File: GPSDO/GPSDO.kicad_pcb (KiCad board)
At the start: 2 copper layers, 39.6 x 27.3 mm, 37 parts, among them J1 analog, J2 Conn_01x03_Pin, J3 USB_B_Mini, J4 1PPSin, SW1 RST#, U1 FT230XS, U2 CH32V003FxPx, U3 TLV9061xDBV, Y2 24 MHz Farnell 4165823

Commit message: 3D model
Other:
- board text added: "CH32V003 GPSDO"
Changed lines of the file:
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@@
 		(tags "SMA THT Female Jack Vertical")
 		(property "Reference" "J4"
-			(at -0.44 -4.56 90)
+			(at 2.54 -5.06 90)
 			(layer "F.SilkS")
 			(effects
@@
 		)
 		(embedded_fonts no)
-		(model "${KICAD10_3DMODEL_DIR}/Connector_Coaxial.3dshapes/SMA_Amphenol_901-144_Vertical.step"
+		(model "${KIPRJMOD}/901-144-8RFX.stp"
 			(offset
-				(xyz 0 0 0)
+				(xyz 0 0 9.5)
 			)
 			(scale
@@
 			)
 			(rotate
-				(xyz 0 0 0)
+				(xyz -0 -90 -0)
 			)
 		)
@@
 		(layer "Edge.Cuts")
 	)
+	(gr_text "CH32V003\nGPSDO"
+		(at 179.28714 83.0016 0)
+		(layer "F.SilkS")
+		(effects
+			(font
+				(size 1.2 1.2)
+				(thickness 0.25)
+				(bold yes)
+			)
+			(justify left bottom)
+		)
+	)
 	(segment

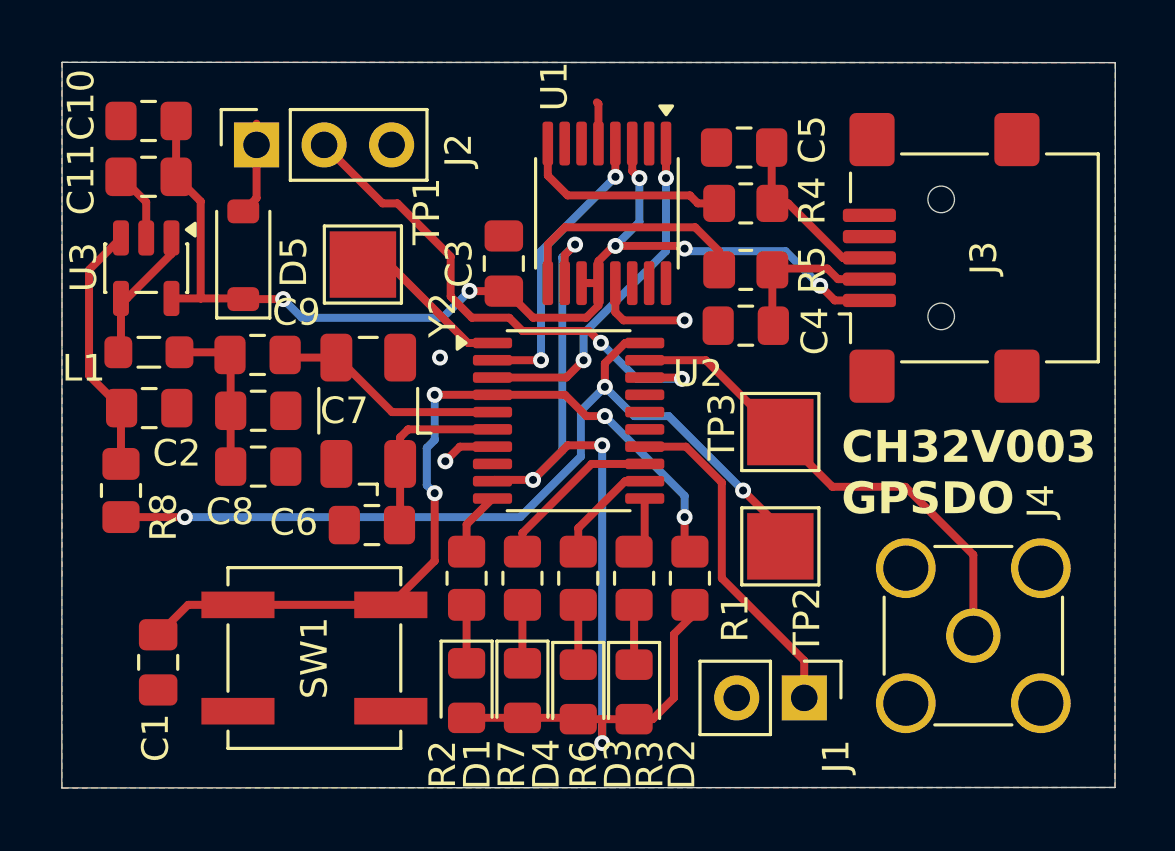
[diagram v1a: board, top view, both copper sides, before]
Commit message: add mounting holes
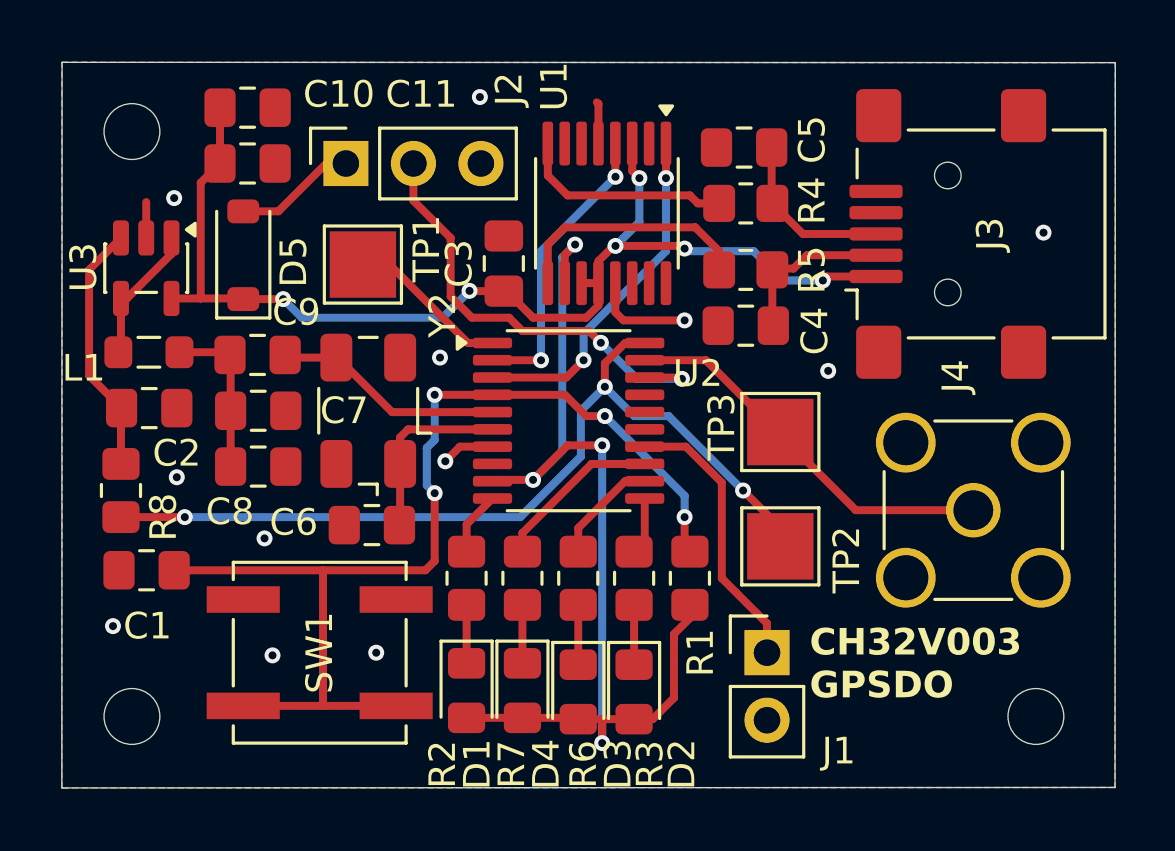
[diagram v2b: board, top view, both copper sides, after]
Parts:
- added H1: MountingHole, MountingHole:MountingHole_2.1mm, F.Cu at (152.6, 68.5)
- added H2: MountingHole, MountingHole:MountingHole_2.1mm, F.Cu at (152.6, 90.5)
- added H3: MountingHole, MountingHole:MountingHole_2.1mm, F.Cu at (186.6, 90.5)
- moved J4 4.72 mm to (184.2, 82.7)
- moved C10 3.76 mm to (156.9, 67.6), turned to 0 degrees
- moved C11 3.76 mm to (156.9, 69.7), turned to 0 degrees
- moved C1 3.49 mm to (153.1, 85.0), turned to 180 degrees
- moved J2 3.43 mm to (160.6, 69.7)
- moved J1 2.20 mm to (176.5, 88.1), turned to 0 degrees
- moved J3 0.93 mm to (183.3, 72.4)
- moved SW1 0.28 mm to (159.7, 88.1), turned to 180 degrees
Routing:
- net Net-(SW1-A): track 31.2 -> 40.5 mm
- net /IC 1PPS: track 18.4 -> 14.7 mm
- net /SWIO: track 19.4 -> 17.0 mm
- net /A2: track 12.8 -> 10.6 mm
- net GND: track 10.1 -> 8.75 mm, vias 3 -> 12

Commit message: rotate analog in
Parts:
- moved J1 3.30 mm to (176.5, 91.4), turned to 90 degrees
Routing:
- net /A2: track 10.6 -> 13.9 mm
- net GND: track 8.75 -> 10.1 mm, vias 12 -> 14
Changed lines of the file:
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@@
 	(footprint "Connector_PinHeader_2.54mm:PinHeader_1x02_P2.54mm_Vertical"
 		(layer "F.Cu")
-		(at 176.48714 88.1016)
+		(at 176.48714 91.4016 90)
 		(descr "Through hole straight pin header, 1x02, 2.54mm pitch, single row")
 		(tags "Through hole pin header THT 1x02 2.54mm single row")
 		(property "Reference" "J1"
-			(at 2.7 3.7 0)
+			(at 2.6 0.9 90)
 			(layer "F.SilkS")
 			(effects
@@
 		)
 		(property "Value" "analog"
-			(at 0 4.92 0)
+			(at 0 4.92 90)
 			(layer "F.Fab")
 			(effects
@@
 		)
 		(property "Datasheet" ""
-			(at 0 0 0)
+			(at 0 0 90)
 			(layer "F.Fab")
 			(hide yes)
@@
 		)
 		(property "Description" "Generic connector, single row, 01x02, script generated"
-			(at 0 0 0)
+			(at 0 0 90)
 			(layer "F.Fab")
 			(hide yes)
@@
 		)
 		(fp_line
-			(start -1.38 1.27)
-			(end -1.38 3.92)
+			(start 1.38 1.27)
+			(end 1.38 3.92)
 			(stroke
 				(width 0.12)
@@
 		)
 		(fp_line
-			(start -1.38 3.92)
-			(end 1.38 3.92)
+			(start -1.38 1.27)
+			(end -1.38 3.92)
 			(stroke
 				(width 0.12)
@@
 		)
 		(fp_line
-			(start 1.38 1.27)
+			(start -1.38 3.92)
 			(end 1.38 3.92)
 			(stroke
@@
 		)
 		(fp_line
-			(start -1.27 -0.635)
-			(end -0.635 -1.27)
+			(start 1.27 -1.27)
+			(end 1.27 3.81)
 			(stroke
 				(width 0.1)
@@
 		)
 		(fp_line
-			(start -1.27 3.81)
-			(end -1.27 -0.635)
+			(start -0.635 -1.27)
+			(end 1.27 -1.27)
 			(stroke
 				(width 0.1)
@@
 		)
 		(fp_line
-			(start -0.635 -1.27)
-			(end 1.27 -1.27)
+			(start -1.27 -0.635)
+			(end -0.635 -1.27)
 			(stroke
 				(width 0.1)
@@
 		)
 		(fp_line
-			(start 1.27 -1.27)
-			(end 1.27 3.81)
+			(start 1.27 3.81)
+			(end -1.27 3.81)
 			(stroke
 				(width 0.1)
@@
 		)
 		(fp_line
-			(start 1.27 3.81)
-			(end -1.27 3.81)
+			(start -1.27 3.81)
+			(end -1.27 -0.635)
 			(stroke
 				(width 0.1)
@@
 		)
 		(fp_text user "${REFERENCE}"
-			(at 0 1.27 90)
+			(at 0 1.27 0)
 			(layer "F.Fab")
 			(effects
@@
 		)
 		(pad "1" thru_hole rect
-			(at 0 0)
+			(at 0 0 90)
 			(size 1.7 1.7)
 			(drill 1)
@@
 		)
 		(pad "2" thru_hole circle
-			(at 0 2.54)
+			(at 0 2.54 90)
 			(size 1.7 1.7)
 			(drill 1)
@@
 	)
 	(gr_text "CH32V003\nGPSDO"
-		(at 178.08714 89.9016 0)
+		(at 178.28714 89.8016 0)
 		(layer "F.SilkS")
 		(effects
@@
 	)
 	(segment
+		(start 167.43714 80.3516)
+		(end 167.48714 80.3016)
+		(width 0.3)
+		(layer "F.Cu")
+		(net "GND")
+	)
+	(segment
 		(start 170.14714 67.4616)
 		(end 170.08714 67.4016)
@@
 	(segment
 		(start 166.16214 80.3516)
+		(end 167.43714 80.3516)
+		(width 0.3)
+		(layer "F.Cu")
+		(net "GND")
+	)
+	(segment
+		(start 166.16214 80.3516)
 		(end 164.93714 80.3516)
 		(width 0.3)
@@
 	)
 	(via
+		(at 173.58714 67.2016)
+		(size 0.6)
+		(drill 0.3)
+		(layers "F.Cu" "B.Cu")
+		(free yes)
+		(net "GND")
+	)
+	(via
 		(at 154.28714 81.5016)
 		(size 0.6)
@@
 	)
 	(via
+		(at 167.48714 80.3016)
+		(size 0.6)
+		(drill 0.3)
+		(layers "F.Cu" "B.Cu")
+		(free yes)
+		(net "GND")
+	)
+	(via
 		(at 178.78714 77.5016)
 		(size 0.6)
@@
 	)
 	(segment
-		(start 173.43714 80.3516)
-		(end 174.78714 81.7016)
+		(start 174.78714 81.7016)
+		(end 174.78714 85.3016)
 		(width 0.3)
 		(layer "F.Cu")
@@
 	)
 	(segment
-		(start 171.88714 80.3516)
-		(end 173.43714 80.3516)
+		(start 173.43714 80.3516)
+		(end 174.78714 81.7016)
 		(width 0.3)
 		(layer "F.Cu")
@@
 	)
 	(segment
-		(start 174.78714 85.3016)
-		(end 176.48714 87.0016)
+		(start 176.48714 87.0016)
+		(end 176.48714 91.4016)
 		(width 0.3)
 		(layer "F.Cu")
@@
 	)
 	(segment
-		(start 176.48714 87.0016)
-		(end 176.48714 88.1016)
+		(start 174.78714 85.3016)
+		(end 176.48714 87.0016)
 		(width 0.3)
 		(layer "F.Cu")
@@
 	)
 	(segment
-		(start 174.78714 81.7016)
-		(end 174.78714 85.3016)
+		(start 171.88714 80.3516)
+		(end 173.43714 80.3516)
 		(width 0.3)
 		(layer "F.Cu")
